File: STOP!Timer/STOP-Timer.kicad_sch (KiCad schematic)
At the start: 6 parts, among them SW1 SW_Push_DPDT, SW2 SW_Push_DPDT, SW3 SW_Push_DPDT, U2 PEC11R-4230F-S0024, U3 PEC11R-4230F-S0024

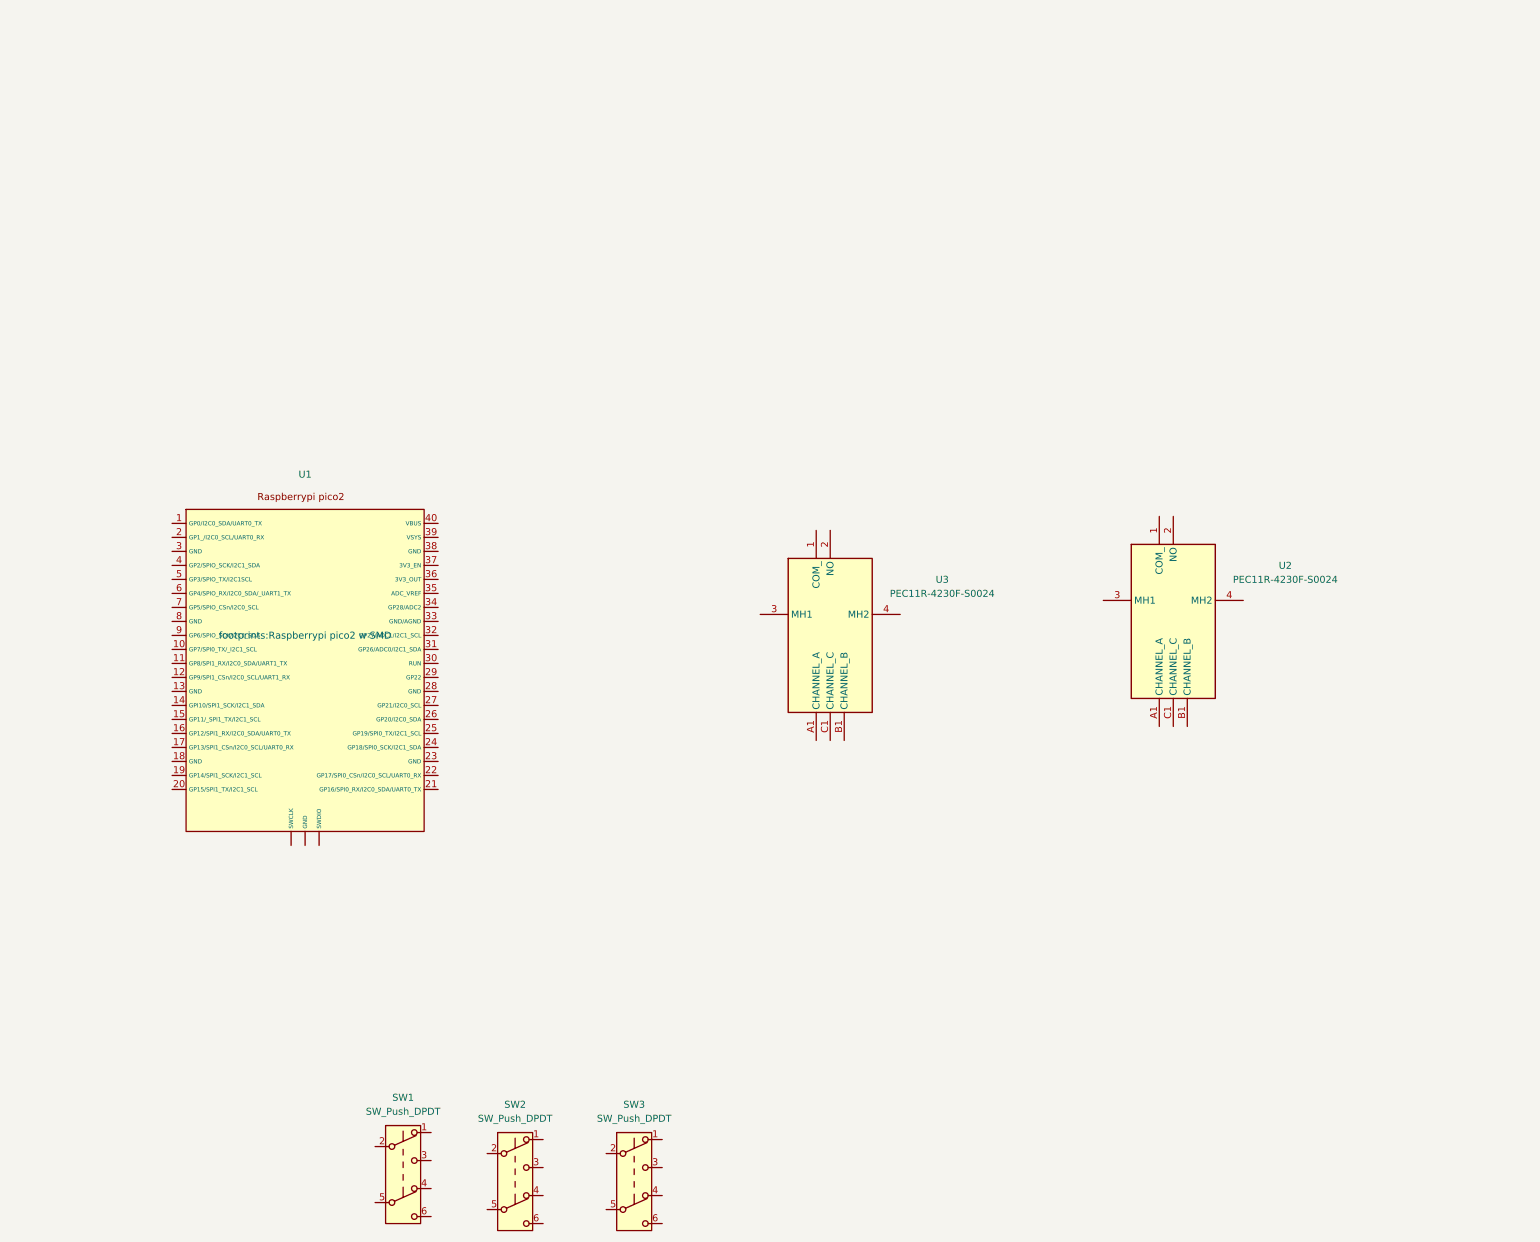
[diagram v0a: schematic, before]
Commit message: Add LCD Circuit
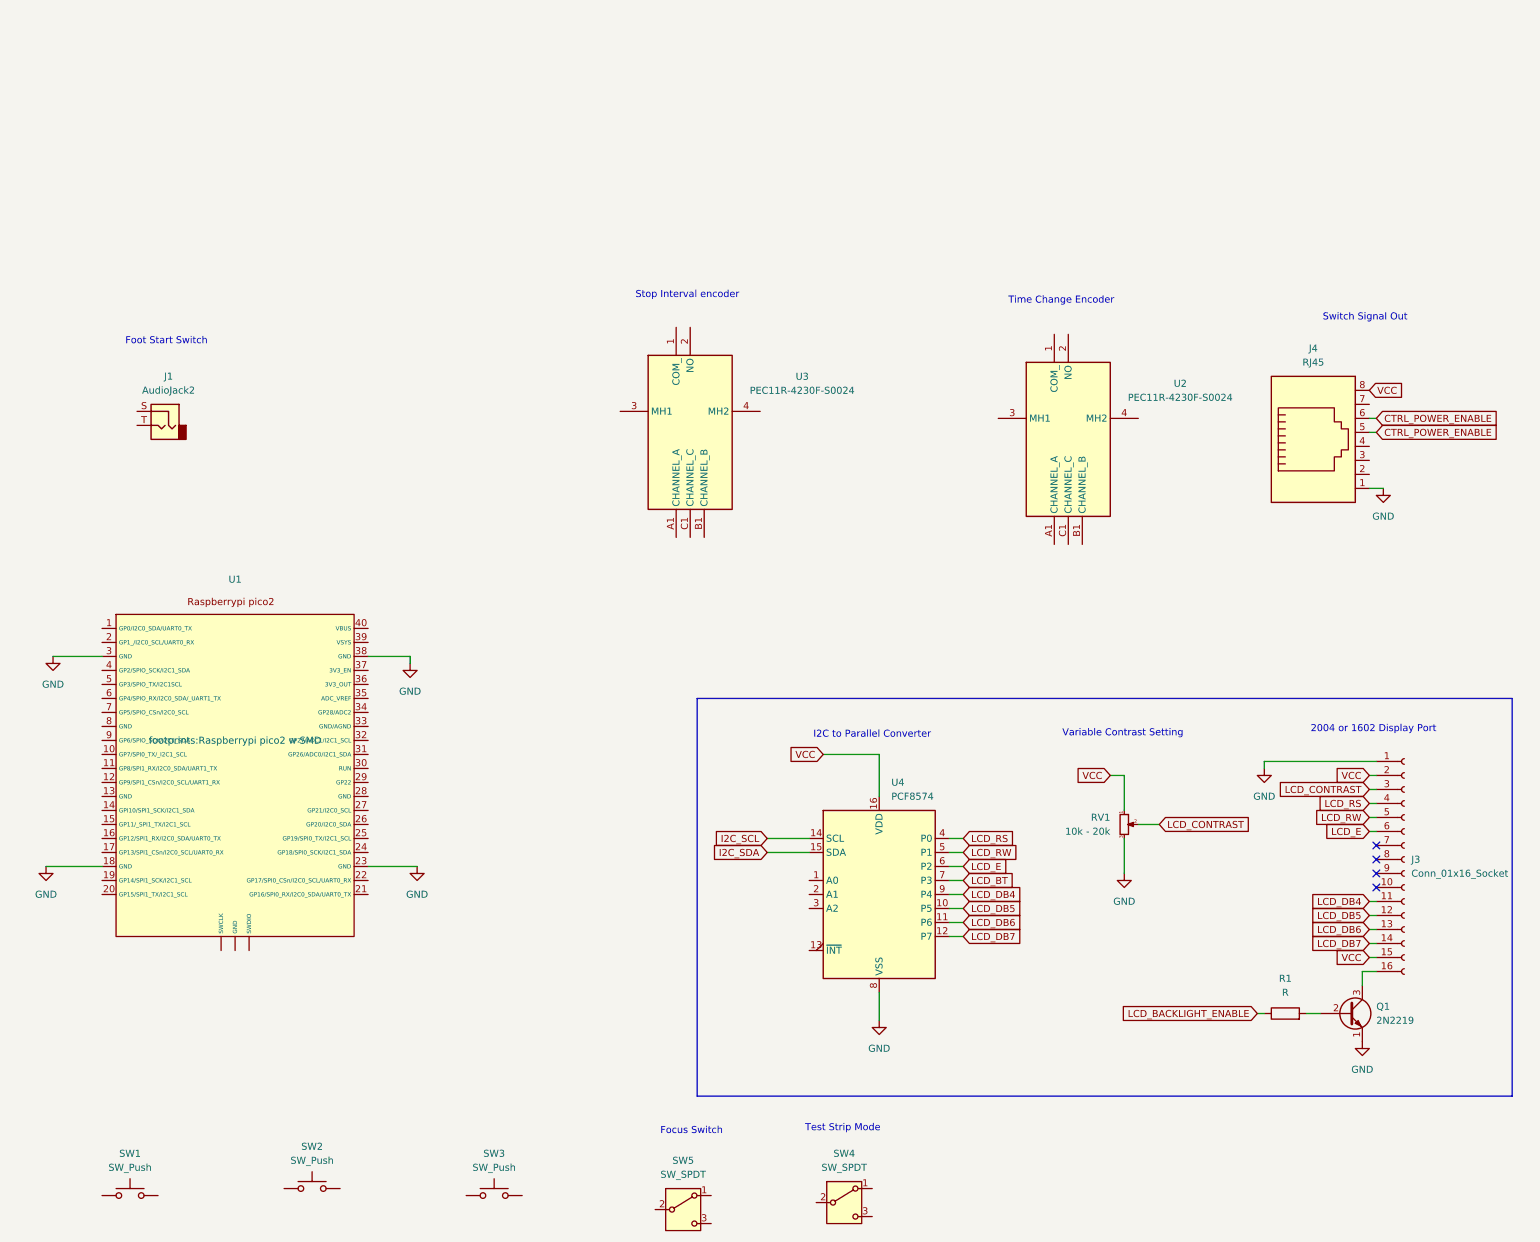
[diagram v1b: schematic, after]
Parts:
- removed SW1, SW2, SW3: SW_Push_DPDT, Button_Switch_THT:SW_Push_2P2T_Toggle_CK_PVA2xxH4xxxxxxV2, symbol Switch:SW_Push_DPDT
- added J1: AudioJack2, symbol Connector_Audio:AudioJack2
- added J3: Conn_01x16_Socket, symbol Connector:Conn_01x16_Socket
- added J4: RJ45, symbol Connector:RJ45
- added Q1: 2N2219, Package_TO_SOT_THT:TO-39-3, symbol Transistor_BJT:2N2219
- added R1: R, symbol Device:R
- added RV1: 10k - 20k, symbol Device:R_Potentiometer_Small
- added SW1, SW2, SW3: SW_Push, symbol Switch:SW_Push
- added SW4, SW5: SW_SPDT, symbol Switch:SW_SPDT
- added U4: PCF8574, symbol Interface_Expansion:PCF8574
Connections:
- net GND: now reaches U1.18 (GND)
- net GND: now also U1.23 (GND), U1.3 (GND), U1.38 (GND), J3.1 (Pin_1), J4.1, Q1.1 (E), RV1.3, U4.8 (VSS)
- new net: Q1.2 (B), R1.2
- new net: J3.16 (Pin_16), Q1.3 (C)
- new net CTRL_POWER_ENABLE: J4.5, J4.6
- new net I2C_SCL: U4.14 (SCL)
- new net I2C_SDA: U4.15 (SDA)
- new net LCD_BACKLIGHT_ENABLE: R1.1
- new net LCD_BT: U4.7 (P3)
- new net LCD_CONTRAST: J3.3 (Pin_3), RV1.2
- new net LCD_DB4: J3.11 (Pin_11), U4.9 (P4)
- new net LCD_DB5: J3.12 (Pin_12), U4.10 (P5)
- new net LCD_DB6: J3.13 (Pin_13), U4.11 (P6)
- new net LCD_DB7: J3.14 (Pin_14), U4.12 (P7)
- new net LCD_E: J3.6 (Pin_6), U4.6 (P2)
- new net LCD_RS: J3.4 (Pin_4), U4.4 (P0)
- new net LCD_RW: J3.5 (Pin_5), U4.5 (P1)
- new net VCC: J3.15 (Pin_15), J3.2 (Pin_2), J4.8, RV1.1, U4.16 (VDD)
- no-connect marks 0 -> 4
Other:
- note added: "2004 or 1602 Display Port"
- note added: "Focus Switch"
- note added: "Foot Start Switch"
- note added: "I2C to Parallel Converter"
- note added: "Stop Interval encoder"
- note added: "Switch Signal Out"
- note added: "Test Strip Mode"
- note added: "Time Change Encoder"
- note added: "Variable Contrast Setting"
- moved on the sheet: U1, U2, U3

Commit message: Move Schematics to seperate sheets + add some Pull Up Resistors
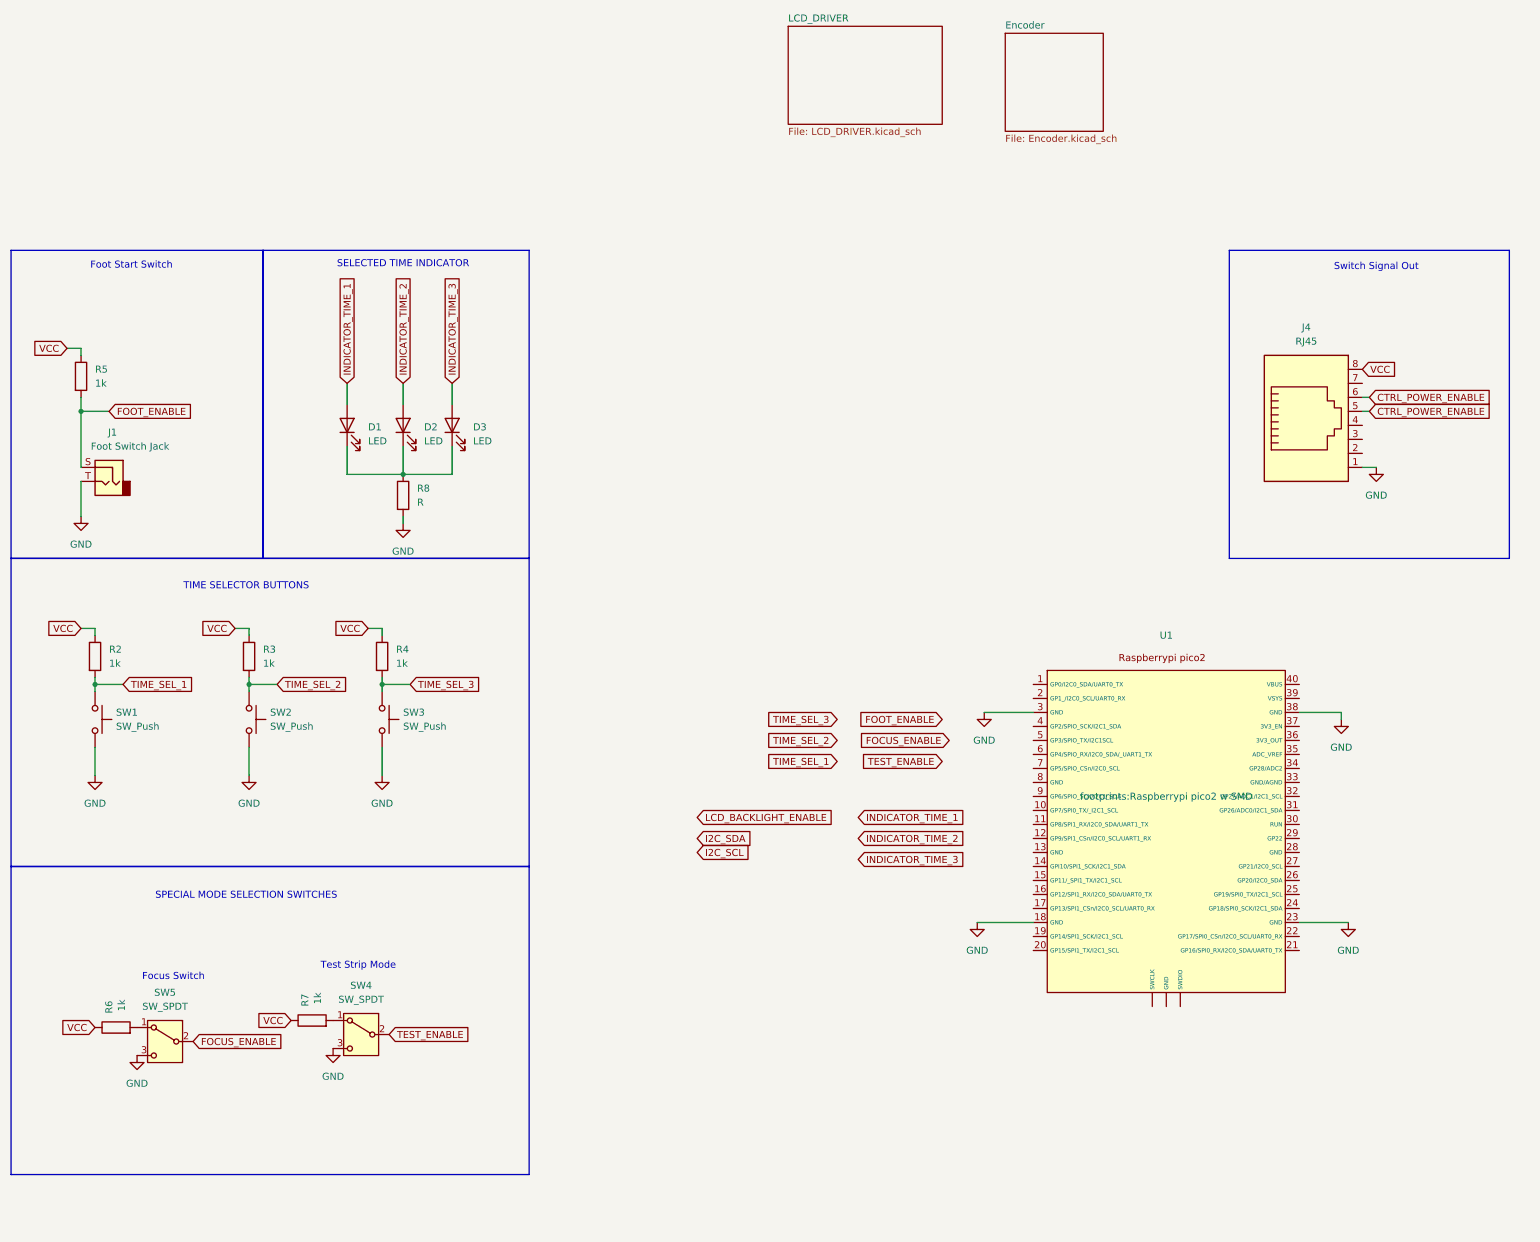
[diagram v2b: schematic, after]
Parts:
- removed J3: Conn_01x16_Socket, symbol Connector:Conn_01x16_Socket
- removed Q1: 2N2219, Package_TO_SOT_THT:TO-39-3, symbol Transistor_BJT:2N2219
- removed R1: R, symbol Device:R
- removed RV1: 10k - 20k, symbol Device:R_Potentiometer_Small
- removed U2, U3: PEC11R-4230F-S0024, project_footprints:PEC11R4225FS0012, symbol PEC11R-4225F-S0012:PEC11R-4225F-S0012
- removed U4: PCF8574, symbol Interface_Expansion:PCF8574
- added D1, D2, D3: LED, symbol Device:LED
- added R2, R3, R4, R5, R6, R7: 1k, symbol Device:R
- added R8: R, symbol Device:R
- J1: value AudioJack2 -> Foot Switch Jack
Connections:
- net GND: now also J1.T, SW1.2, SW2.2, SW3.2, SW4.3 (C), SW5.3 (C), R8.2
- net VCC: now also R2.1, R3.1, R4.1, R5.1, R6.1, R7.1
- net TIME_SEL_3: now reaches SW3.1
- net TIME_SEL_3: now also R4.2
- net at SW4.1 (A): now also R7.2
- net TEST_ENABLE: now reaches SW4.2 (B)
- net TIME_SEL_1: now reaches SW1.1
- net TIME_SEL_1: now also R2.2
- net FOOT_ENABLE: now reaches J1.S
- net FOOT_ENABLE: now also R5.2
- net TIME_SEL_2: now reaches SW2.1
- net TIME_SEL_2: now also R3.2
- net at SW5.1 (A): now also R6.2
- net FOCUS_ENABLE: now reaches SW5.2 (B)
- new net: D1.1 (K), D2.1 (K), D3.1 (K), R8.1
- new net INDICATOR_TIME_1: D1.2 (A)
- new net INDICATOR_TIME_2: D2.2 (A)
- new net INDICATOR_TIME_3: D3.2 (A)
- no-connect marks 4 -> 0
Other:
- added sheet Encoder (Encoder.kicad_sch)
- added sheet LCD_DRIVER (LCD_DRIVER.kicad_sch)
- note added: "SELECTED TIME INDICATOR"
- note added: "SPECIAL MODE SELECTION SWITCHES"
- note added: "TIME SELECTOR BUTTONS"
- note removed: "2004 or 1602 Display Port"
- note removed: "I2C to Parallel Converter"
- note removed: "Stop Interval encoder"
- note removed: "Time Change Encoder"
- note removed: "Variable Contrast Setting"
- moved on the sheet: J1, J4, SW1, SW5, U1

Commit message: Update Schematic
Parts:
- removed J4: RJ45, symbol Connector:RJ45
- removed SW4: SW_SPDT, symbol Switch:SW_SPDT
- added BZ1: Buzzer, Buzzer_Beeper:Buzzer_12x9.5RM7.6, symbol Device:Buzzer
- added J3: XLR3, Connector_Audio:Jack_XLR_Neutrik_NC3FAAH-0_Horizontal, symbol Connector_Audio:XLR3
- added R10, R11, R9: 1k, Resistor_SMD:R_0805_2012Metric_Pad1.20x1.40mm_HandSolder, symbol Device:R
- added SW4, SW6, SW7: SW_Push, Button_Switch_Keyboard:SW_Cherry_MX_1.50u_PCB, symbol Switch:SW_Push
- added SW8: SW_SPDT, symbol Switch:SW_SPDT
- added U2: EC11E18244AU, Rotary_Encoder:RotaryEncoder_Alps_EC11E-Switch_Vertical_H20mm, symbol project:EC11E18244AU
- D1, D2, D3: footprint (none) -> LED_SMD:LED_0805_2012Metric_Pad1.15x1.40mm_HandSolder
- J1: footprint (none) -> Connector_Audio:Jack_6.35mm_Neutrik_NMJ4HCD2_Horizontal
- R2, R3, R4, R5, R6, R7, R8: footprint (none) -> Resistor_SMD:R_0805_2012Metric_Pad1.20x1.40mm_HandSolder
- SW1, SW2, SW3: footprint (none) -> Button_Switch_Keyboard:SW_Cherry_MX_1.50u_PCB; JLC (none) -> C49234237
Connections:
- net CTRL_POWER_ENABLE: now also J3.3
- net GND: now also BZ1.2 (-), J3.2, SW4.2, SW6.2, SW7.2, U2.E1 (NO)
- net VCC: now also U1.40 (VBUS), J3.1, R10.1, R11.1, R9.1
- net MODE_SEL: now reaches R7.2
- net MODE_SEL: now also SW4.1
- new net: BZ1.1 (+), SW8.2 (B)
- new net BUZZ_SIGNAL: SW8.1 (A)
- new net ENCODER_A: U2.A1
- new net ENCODER_B: U2.B1
- new net ENCODER_SEL: R11.2, U2.D1 (COM)
- new net START_SEL: R10.2, SW7.1
- new net VIEW_SEL: R9.2, SW6.1
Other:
- removed sheet Encoder
- note added: "MENU ENCODER"
- note removed: "Test Strip Mode"
- moved on the sheet: R6, SW5

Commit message: Update 31 03 2026
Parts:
- added H1, H2, H3, H4: MountingHole_Pad, MountingHole:MountingHole_3.2mm_M3_DIN965_Pad, symbol Mechanical:MountingHole_Pad
- added J2, J4: Conn_01x04_Pin, Connector_PinHeader_2.54mm:PinHeader_1x04_P2.54mm_Vertical, symbol Connector:Conn_01x04_Pin
- added Q2: AO3401A, Package_TO_SOT_SMD:SOT-23, symbol Transistor_FET:AO3401A
- added R1: 4.7k, Resistor_SMD:R_0805_2012Metric_Pad1.20x1.40mm_HandSolder, symbol Device:R
- J1: footprint Connector_Audio:Jack_6.35mm_Neutrik_NMJ4HCD2_Horizontal -> Connector_Audio:Jack_6.35mm_Neutrik_NMJ4HFD2_Horizontal
- J3: footprint Connector_Audio:Jack_XLR_Neutrik_NC3FAAH-0_Horizontal -> Connector_Audio:Jack_XLR_Neutrik_NC3MAAH-0_Horizontal
- R10: value 1k -> 4.7k
- SW1, SW2, SW3, SW4, SW6, SW7: footprint Button_Switch_Keyboard:SW_Cherry_MX_1.50u_PCB -> project_footprints:SW_Cherry_MX_1.50u_PCB_3dmodel
- SW8: footprint (none) -> Button_Switch_SMD:SW_SPDT_PCM12; JLC (none) -> C221841
- U2: footprint Rotary_Encoder:RotaryEncoder_Alps_EC11E-Switch_Vertical_H20mm -> project_footprints:EC11E18244AU
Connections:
- net FOOT_ENABLE is gone; now on net START_SEL: J1.S, R5.2
- net BUZZ_SIGNAL: now also U1.39 (VSYS)
- net CTRL_POWER_ENABLE: now also U1.16 (GP12/SPI1_RX/I2C0_SDA/UART0_TX), Q2.1 (G); no longer J3.3
- net ENCODER_A: now also U1.4 (GP2/SPIO_SCK/I2C1_SDA)
- net ENCODER_B: now also U1.5 (GP3/SPIO_TX/I2C1SCL)
- net GND: now also R10.2, U1.33 (GND/AGND), U1.8 (GND), H1.1, H2.1, H3.1, H4.1, J2.4 (Pin_4); no longer R8.2
- net I2C_SCL: now also U1.27 (GP21/I2C0_SCL), R1.2
- net I2C_SDA: now also R10.1, U1.26 (GP20/I2C0_SDA)
- net INDICATOR_TIME_1: now also U1.20 (GP15/SPI1_TX/I2C1_SCL), J2.1 (Pin_1); no longer D1.2 (A)
- net INDICATOR_TIME_2: now also U1.19 (GP14/SPI1_SCK/I2C1_SCL), J2.2 (Pin_2); no longer D2.2 (A)
- net INDICATOR_TIME_3: now also U1.17 (GP13/SPI1_CSn/I2C0_SCL/UART0_RX), J2.3 (Pin_3); no longer D3.2 (A)
- net LCD_BACKLIGHT_ENABLE: now also U1.32 (GP27/ADC1/I2C1_SCL)
- net MODE_SEL: now also U1.9 (GP6/SPIO_SCK/I2C1_SDA)
- net START_SEL: now also U1.10 (GP7/SPI0_TX/_I2C1_SCL); no longer R10.2
- net TIME_SEL_1: now also U1.11 (GP8/SPI1_RX/I2C0_SDA/UART1_TX)
- net TIME_SEL_2: now also U1.12 (GP9/SPI1_CSn/I2C0_SCL/UART1_RX)
- net TIME_SEL_3: now also U1.13 (GND)
- net VCC: now also Q2.3 (D), R1.1; no longer R10.1
- net VIEW_SEL: now also U1.7 (GP5/SPIO_CSn/I2C0_SCL)
- new net: D2.2 (A), J4.2 (Pin_2)
- new net: J4.4 (Pin_4), R8.2
- new net: D3.2 (A), J4.3 (Pin_3)
- new net: D1.2 (A), J4.1 (Pin_1)
- new net: J3.3, Q2.2 (S)
- no-connect marks 0 -> 24
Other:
- note added: "CONNECTOR TO FRONT PANEL BOARD"
- moved on the sheet: J1, R5, SW7

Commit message: Change Look of Board
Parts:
- J4: footprint Connector_PinHeader_2.54mm:PinHeader_1x04_P2.54mm_Vertical -> Connector_PinSocket_2.54mm:PinSocket_1x04_P2.54mm_Vertical
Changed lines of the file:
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@@
 			)
 		)
-		(property "Footprint" "Connector_PinHeader_2.54mm:PinHeader_1x04_P2.54mm_Vertical"
+		(property "Footprint" "Connector_PinSocket_2.54mm:PinSocket_1x04_P2.54mm_Vertical"
 			(at 83.82 24.13 0)
 			(effects

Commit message: update to order version 1.0
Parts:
- removed R11, R2, R3, R4, R5, R7, R9: 1k, Resistor_SMD:R_0805_2012Metric_Pad1.20x1.40mm_HandSolder, symbol Device:R
- BZ1: JLC (none) -> C2877
- J1: footprint Connector_Audio:Jack_6.35mm_Neutrik_NMJ4HFD2_Horizontal -> project_footprints:NEUTRIK NMJ2HF-S
- J3: JLC (none) -> C368470
- R1, R10: JLC (none) -> C17673
- R6: JLC (none) -> C2907295
- U1: JLC (none) -> C41407547
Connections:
- net BUZZ_SIGNAL: now also U1.34 (GP28/ADC2); no longer U1.39 (VSYS)
- net ENCODER_SEL: now also U1.6 (GP4/SPIO_RX/I2C0_SDA/_UART1_TX)
- net GND: now also U2.C1
- net VCC: now also U1.39 (VSYS); no longer U1.40 (VBUS)
- no-connect marks 24 -> 21
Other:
- moved on the sheet: U2
